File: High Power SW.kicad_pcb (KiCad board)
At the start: 2 copper layers, 48 x 36 mm, 21 parts, among them CN1 Jumper_NC_Small, Q1 PSMN5R6-60YLX, U1 PS2801C-1-A

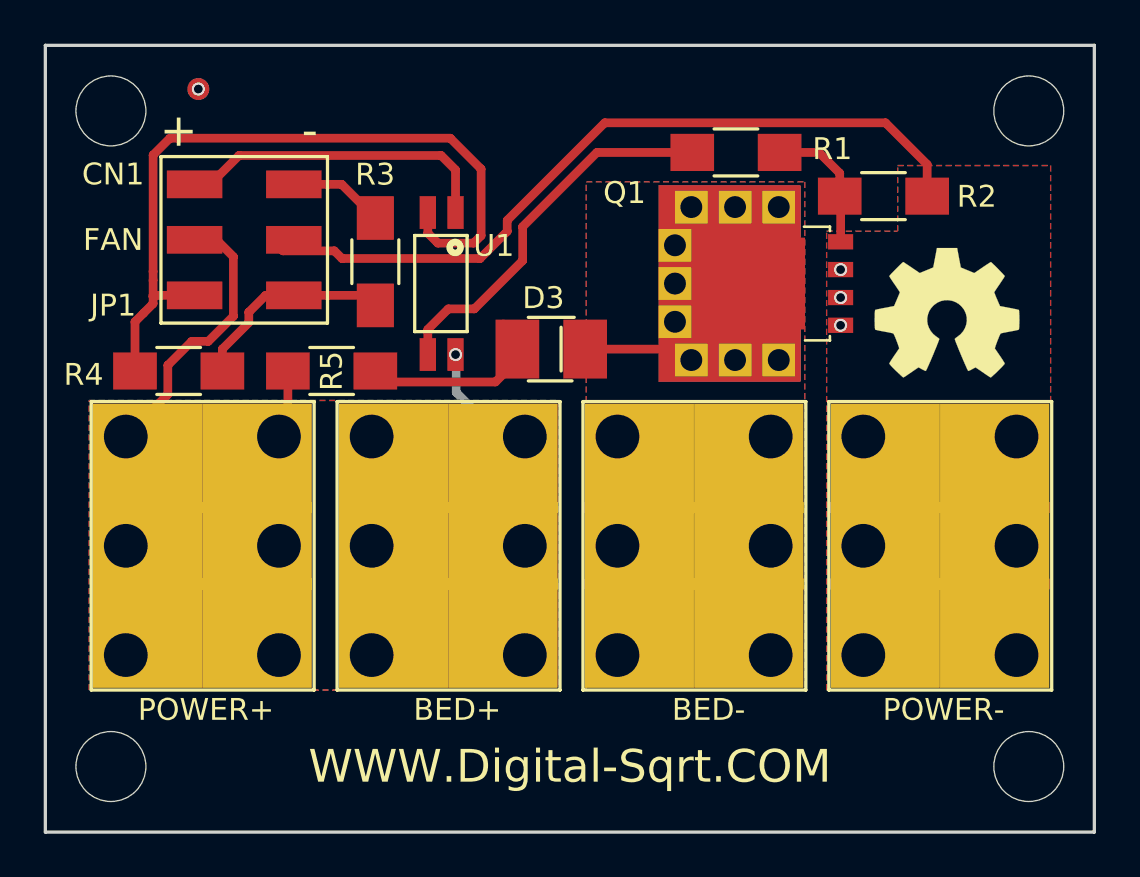
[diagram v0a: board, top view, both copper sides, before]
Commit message: Update Driver based on feedback
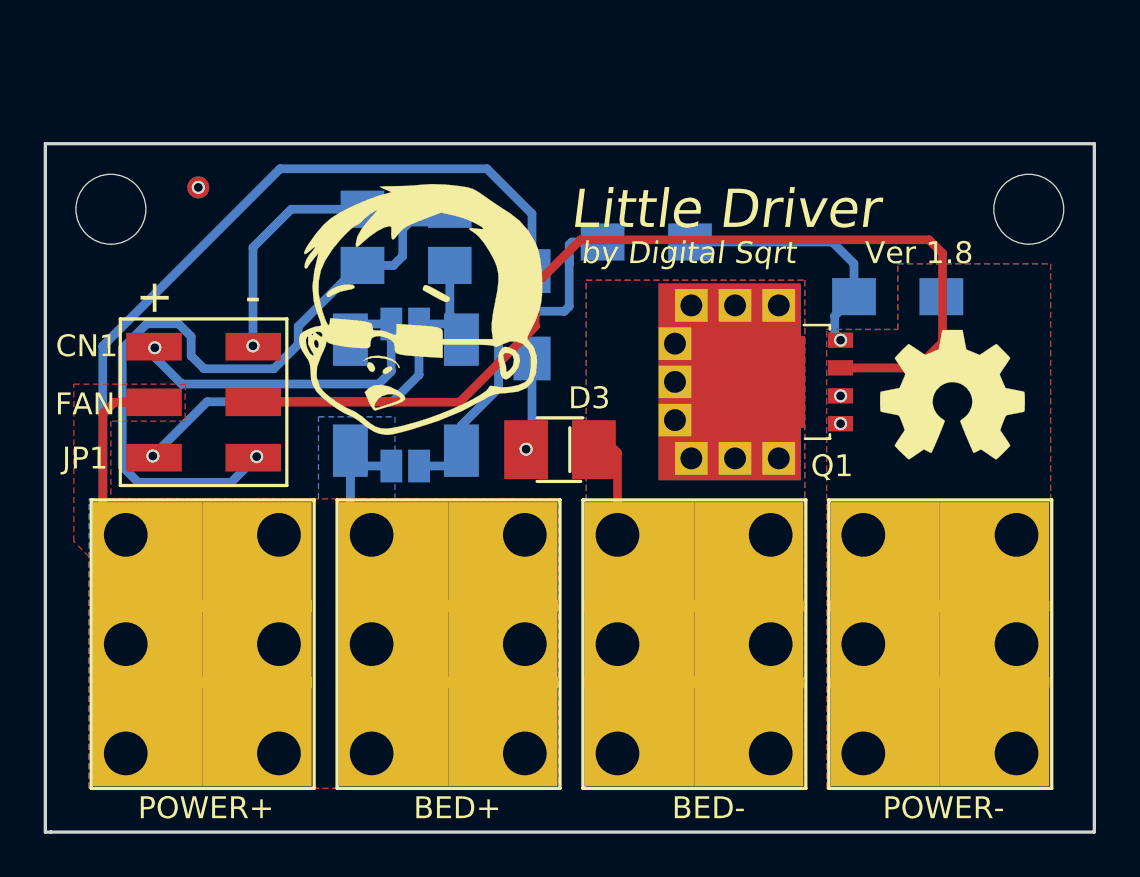
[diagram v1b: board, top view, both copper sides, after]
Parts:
- removed the ? at (70.0, 136.0)
- removed the ? at (112.0, 136.0)
- ?: moved to F.Cu
- R1, R2, R3, R4, R5: moved to B.Cu
- U1: footprint MyLib:SOP-4 -> MyLib:OP_Hybrid; moved to B.Cu
- moved R4 11.5 mm to (83.5, 113.1), turned to 0 degrees
- moved R5 9.52 mm to (89.3, 115.3), turned to 270 degrees
- moved CN1 7.66 mm to (74.2, 119.3)
- moved R1 5.80 mm to (94.5, 112.0)
- moved ? 5.78 mm to (84.0, 115.0), turned to 0 degrees
- moved U1 5.35 mm to (83.5, 119.0)
- moved R2 4.65 mm to (106.0, 114.5)
- moved D3 4.62 mm to (90.5, 121.5)
- moved ? 4.50 mm to (112.0, 110.5)
- moved ? 4.50 mm to (70.0, 110.5)
- moved BED+ 4.50 mm to (85.3, 130.4)
- moved BED- 4.50 mm to (96.6, 130.4)
- moved F1  4.50 mm to (74.0, 109.5) (x2)
- moved POWER+ 4.50 mm to (74.1, 130.4)
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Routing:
- net +BATT: track 23.3 -> 51.5 mm, vias 1 -> 0
- net Net-(JP1-Pad2): track 9.93 -> 36.2 mm, vias 0 -> 1
- net Net-(JP1-Pad1): track 37.8 -> 23.7 mm, vias 0 -> 1
- net GND: track 37.3 -> 46.3 mm, vias 4 -> 3
- net Net-(CN1-Pad2): track 5.37 -> 11.3 mm, vias 0 -> 1
- net Net-(Q1-Pad4): track 6.30 -> 11.9 mm, vias 0 -> 1
- net Net-(D3-Pad2): track 9.71 -> 4.77 mm, vias 0 -> 1
- net Net-(CN1-Pad1): track 13.9 -> 17.3 mm, vias 0 -> 1
- net Net-(BED-1-Pad1): track 5.57 -> 6.11 mm
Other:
- board size 48 x 36 mm -> 48 x 31.5 mm
- board text added: "by Digital Sqrt"
- board text removed: "Clearance Hole for M3"
- board text removed: "Digital Sqrt"
